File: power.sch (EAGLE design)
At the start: 22 parts

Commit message: change all the things
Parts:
- removed TP1, TP2, TP3, TP4: TPPAD1-13Y, testpad:TPPAD1-13Y
- added BAT+, BAT-, H1, H2, PV+, PV-: MOUNT-PAD-ROUND2.8, holes:MOUNT-PAD-ROUND2.8
- added R10: 1k, rcl:R-US_R0603
- added R9: 47k, rcl:R-US_R0603
- R1, R2: value (none) -> 0R1
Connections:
- new net N$18: R10.2, R9.2, U$6.AIN4
- new net N$8: R9.1
- net GND: now also H1.MOUNT, H2.MOUNT, R10.1
- net N$14: now also BAT-.MOUNT; no longer TP4.TP
- net N$16: now also PV-.MOUNT; no longer TP2.TP
- net N$3: now also PV+.MOUNT, U$3.P$2; no longer TP1.TP, U$3.P$1
- net N$6: now also U$3.P$1; no longer U$3.P$2
- net N$7: now also BAT+.MOUNT; no longer TP3.TP
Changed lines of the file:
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@@
 </classes>
 <parts>
-<part name="TP1" library="testpad" deviceset="TP" device="PAD1-13Y"/>
-<part name="TP2" library="testpad" deviceset="TP" device="PAD1-13Y"/>
-<part name="TP3" library="testpad" deviceset="TP" device="PAD1-13Y"/>
-<part name="TP4" library="testpad" deviceset="TP" device="PAD1-13Y"/>
 <part name="D1" library="diode" deviceset="BY500" device=""/>
 <part name="D2" library="diode" deviceset="BY500" device=""/>
@@
 <part name="U$1" library="mjg" deviceset="FDB6670AL" device=""/>
 <part name="U$2" library="mjg" deviceset="FDB6670AL" device=""/>
-<part name="R1" library="rcl" deviceset="R-US_" device="R0603"/>
-<part name="R2" library="rcl" deviceset="R-US_" device="R0603"/>
+<part name="R1" library="rcl" deviceset="R-US_" device="R0603" value="0R1"/>
+<part name="R2" library="rcl" deviceset="R-US_" device="R0603" value="0R1"/>
 <part name="U$3" library="chokes" deviceset="PLH10AN2211R5P2B" device=""/>
 <part name="U$4" library="chokes" deviceset="TLF14CBH3321R0K1" device=""/>
@@
 <part name="R8" library="rcl" deviceset="R-US_" device="R0603" value="1k"/>
 <part name="GND4" library="supply1" deviceset="GND" device=""/>
+<part name="R9" library="rcl" deviceset="R-US_" device="R0603" value="47k"/>
+<part name="R10" library="rcl" deviceset="R-US_" device="R0603" value="1k"/>
+<part name="GND5" library="supply1" deviceset="GND" device=""/>
+<part name="PV+" library="holes" deviceset="MOUNT-PAD-ROUND" device="2.8"/>
+<part name="PV-" library="holes" deviceset="MOUNT-PAD-ROUND" device="2.8"/>
+<part name="BAT+" library="holes" deviceset="MOUNT-PAD-ROUND" device="2.8"/>
+<part name="BAT-" library="holes" deviceset="MOUNT-PAD-ROUND" device="2.8"/>
+<part name="H1" library="holes" deviceset="MOUNT-PAD-ROUND" device="2.8"/>
+<part name="H2" library="holes" deviceset="MOUNT-PAD-ROUND" device="2.8"/>
+<part name="GND6" library="supply1" deviceset="GND" device=""/>
 </parts>
 <sheets>
@@
 </plain>
 <instances>
-<instance part="TP1" gate="G$1" x="2.54" y="43.18" rot="R90"/>
-<instance part="TP2" gate="G$1" x="-12.7" y="5.08" rot="R90"/>
-<instance part="TP3" gate="G$1" x="96.52" y="58.42" rot="R270"/>
-<instance part="TP4" gate="G$1" x="96.52" y="50.8" rot="R270"/>
 <instance part="D1" gate="1" x="58.42" y="76.2"/>
 <instance part="D2" gate="1" x="58.42" y="71.12"/>
@@
 <instance part="R8" gate="G$1" x="66.04" y="17.78" rot="R180"/>
 <instance part="GND4" gate="1" x="76.2" y="15.24"/>
+<instance part="R9" gate="G$1" x="2.54" y="-7.62" rot="R180"/>
+<instance part="R10" gate="G$1" x="2.54" y="-15.24" rot="R180"/>
+<instance part="GND5" gate="1" x="12.7" y="-17.78"/>
+<instance part="PV+" gate="G$1" x="0" y="43.18" rot="R180"/>
+<instance part="PV-" gate="G$1" x="-12.7" y="5.08" rot="R180"/>
+<instance part="BAT+" gate="G$1" x="96.52" y="58.42"/>
+<instance part="BAT-" gate="G$1" x="96.52" y="50.8"/>
+<instance part="H1" gate="G$1" x="83.82" y="76.2"/>
+<instance part="H2" gate="G$1" x="83.82" y="71.12"/>
+<instance part="GND6" gate="1" x="78.74" y="66.04"/>
 </instances>
 <busses>
@@
 <net name="N$3" class="0">
 <segment>
-<pinref part="TP1" gate="G$1" pin="TP"/>
-<wire x1="12.7" y1="43.18" x2="7.62" y2="43.18" width="0.1524" layer="91"/>
-<pinref part="U$3" gate="G$1" pin="P$1"/>
 <pinref part="R3" gate="G$1" pin="1"/>
-<wire x1="7.62" y1="43.18" x2="5.08" y2="43.18" width="0.1524" layer="91"/>
-<wire x1="7.62" y1="43.18" x2="7.62" y2="33.02" width="0.1524" layer="91"/>
+<wire x1="7.62" y1="43.18" x2="2.54" y2="43.18" width="0.1524" layer="91"/>
+<wire x1="7.62" y1="43.18" x2="7.62" y2="40.64" width="0.1524" layer="91"/>
+<wire x1="7.62" y1="40.64" x2="7.62" y2="33.02" width="0.1524" layer="91"/>
 <wire x1="7.62" y1="33.02" x2="2.54" y2="33.02" width="0.1524" layer="91"/>
-<junction x="7.62" y="43.18"/>
+<wire x1="7.62" y1="40.64" x2="22.86" y2="40.64" width="0.1524" layer="91"/>
+<junction x="7.62" y="40.64"/>
+<pinref part="U$3" gate="G$1" pin="P$2"/>
+<wire x1="22.86" y1="40.64" x2="22.86" y2="43.18" width="0.1524" layer="91"/>
+<pinref part="PV+" gate="G$1" pin="MOUNT"/>
 </segment>
 </net>
@@
 <net name="N$14" class="0">
 <segment>
-<pinref part="TP4" gate="G$1" pin="TP"/>
 <pinref part="R1" gate="G$1" pin="2"/>
 <wire x1="88.9" y1="50.8" x2="91.44" y2="50.8" width="0.1524" layer="91"/>
@@
 <wire x1="91.44" y1="50.8" x2="91.44" y2="-30.48" width="0.1524" layer="91"/>
 <wire x1="91.44" y1="-30.48" x2="124.46" y2="-30.48" width="0.1524" layer="91"/>
+<pinref part="BAT-" gate="G$1" pin="MOUNT"/>
 </segment>
 </net>
@@
 <net name="N$6" class="0">
 <segment>
-<pinref part="U$3" gate="G$1" pin="P$2"/>
-<wire x1="22.86" y1="43.18" x2="27.94" y2="43.18" width="0.1524" layer="91"/>
 <pinref part="U$5" gate="G$1" pin="P$2"/>
 <wire x1="30.48" y1="55.88" x2="27.94" y2="55.88" width="0.1524" layer="91"/>
 <wire x1="27.94" y1="55.88" x2="27.94" y2="45.72" width="0.1524" layer="91"/>
 <pinref part="U$4" gate="G$1" pin="P$1"/>
-<wire x1="27.94" y1="45.72" x2="27.94" y2="43.18" width="0.1524" layer="91"/>
 <wire x1="27.94" y1="45.72" x2="30.48" y2="45.72" width="0.1524" layer="91"/>
 <junction x="27.94" y="45.72"/>
+<wire x1="27.94" y1="45.72" x2="27.94" y2="38.1" width="0.1524" layer="91"/>
+<wire x1="27.94" y1="38.1" x2="12.7" y2="38.1" width="0.1524" layer="91"/>
+<pinref part="U$3" gate="G$1" pin="P$1"/>
+<wire x1="12.7" y1="38.1" x2="12.7" y2="43.18" width="0.1524" layer="91"/>
 </segment>
 </net>
@@
 <pinref part="GND4" gate="1" pin="GND"/>
 </segment>
+<segment>
+<pinref part="R10" gate="G$1" pin="1"/>
+<wire x1="7.62" y1="-15.24" x2="12.7" y2="-15.24" width="0.1524" layer="91"/>
+<pinref part="GND5" gate="1" pin="GND"/>
+</segment>
+<segment>
+<pinref part="H1" gate="G$1" pin="MOUNT"/>
+<pinref part="GND6" gate="1" pin="GND"/>
+<wire x1="81.28" y1="76.2" x2="78.74" y2="76.2" width="0.1524" layer="91"/>
+<wire x1="78.74" y1="76.2" x2="78.74" y2="71.12" width="0.1524" layer="91"/>
+<pinref part="H2" gate="G$1" pin="MOUNT"/>
+<wire x1="78.74" y1="71.12" x2="78.74" y2="68.58" width="0.1524" layer="91"/>
+<wire x1="81.28" y1="71.12" x2="78.74" y2="71.12" width="0.1524" layer="91"/>
+<junction x="78.74" y="71.12"/>
+</segment>
 </net>
 <net name="N$4" class="0">
@@
 <wire x1="-5.08" y1="5.08" x2="-2.54" y2="5.08" width="0.1524" layer="91"/>
 <wire x1="-5.08" y1="-7.62" x2="-5.08" y2="5.08" width="0.1524" layer="91"/>
-<pinref part="TP2" gate="G$1" pin="TP"/>
 <wire x1="-5.08" y1="5.08" x2="-10.16" y2="5.08" width="0.1524" layer="91"/>
 <junction x="-5.08" y="5.08"/>
+<pinref part="PV-" gate="G$1" pin="MOUNT"/>
 </segment>
 </net>
@@
 <pinref part="D1" gate="1" pin="C"/>
 <wire x1="60.96" y1="76.2" x2="68.58" y2="76.2" width="0.1524" layer="91"/>
-<pinref part="TP3" gate="G$1" pin="TP"/>
 <wire x1="68.58" y1="76.2" x2="68.58" y2="71.12" width="0.1524" layer="91"/>
 <pinref part="D2" gate="1" pin="C"/>
@@
 <wire x1="76.2" y1="25.4" x2="76.2" y2="58.42" width="0.1524" layer="91"/>
 <junction x="76.2" y="58.42"/>
+<pinref part="BAT+" gate="G$1" pin="MOUNT"/>
 </segment>
 </net>
@@
 </segment>
 </net>
+<net name="N$8" class="0">
+<segment>
+<pinref part="R9" gate="G$1" pin="1"/>
+<wire x1="12.7" y1="-7.62" x2="7.62" y2="-7.62" width="0.1524" layer="91"/>
+<wire x1="12.7" y1="-7.62" x2="12.7" y2="5.08" width="0.1524" layer="91"/>
+</segment>
+</net>
+<net name="N$18" class="0">
+<segment>
+<wire x1="-2.54" y1="-10.16" x2="109.22" y2="-10.16" width="0.1524" layer="91"/>
+<pinref part="U$6" gate="G$1" pin="AIN4"/>
+<wire x1="109.22" y1="-10.16" x2="109.22" y2="-25.4" width="0.1524" layer="91"/>
+<wire x1="109.22" y1="-25.4" x2="124.46" y2="-25.4" width="0.1524" layer="91"/>
+<pinref part="R9" gate="G$1" pin="2"/>
+<wire x1="-2.54" y1="-7.62" x2="-2.54" y2="-10.16" width="0.1524" layer="91"/>
+<pinref part="R10" gate="G$1" pin="2"/>
+<wire x1="-2.54" y1="-15.24" x2="-2.54" y2="-10.16" width="0.1524" layer="91"/>
+<junction x="-2.54" y="-10.16"/>
+</segment>
+</net>

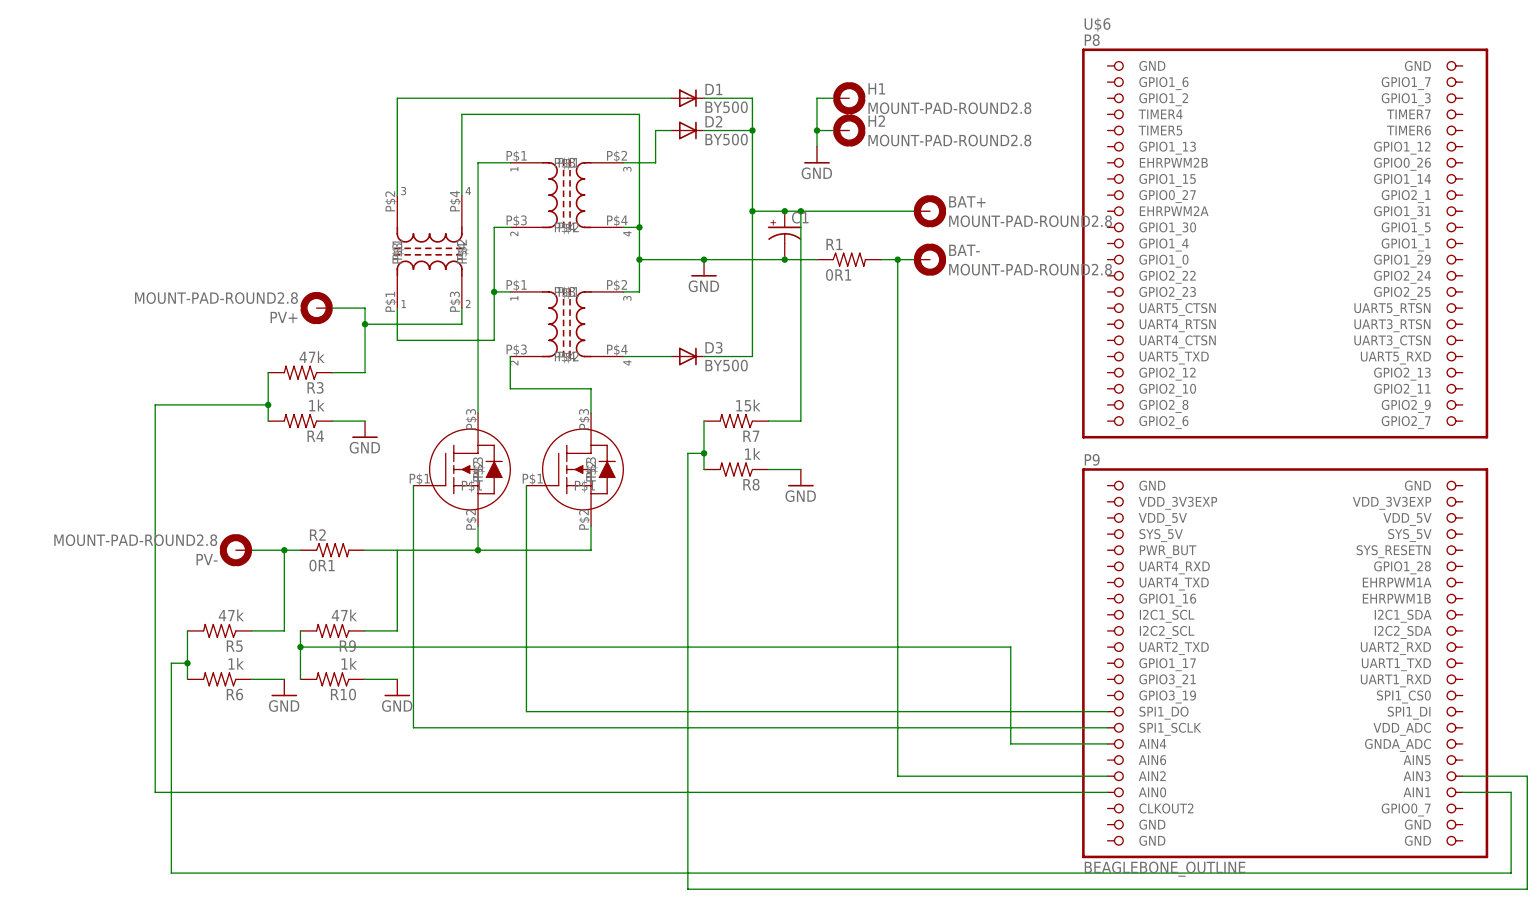
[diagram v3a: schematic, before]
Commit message: schematic might be correct.  board is routed.  no idea if it's routed well.
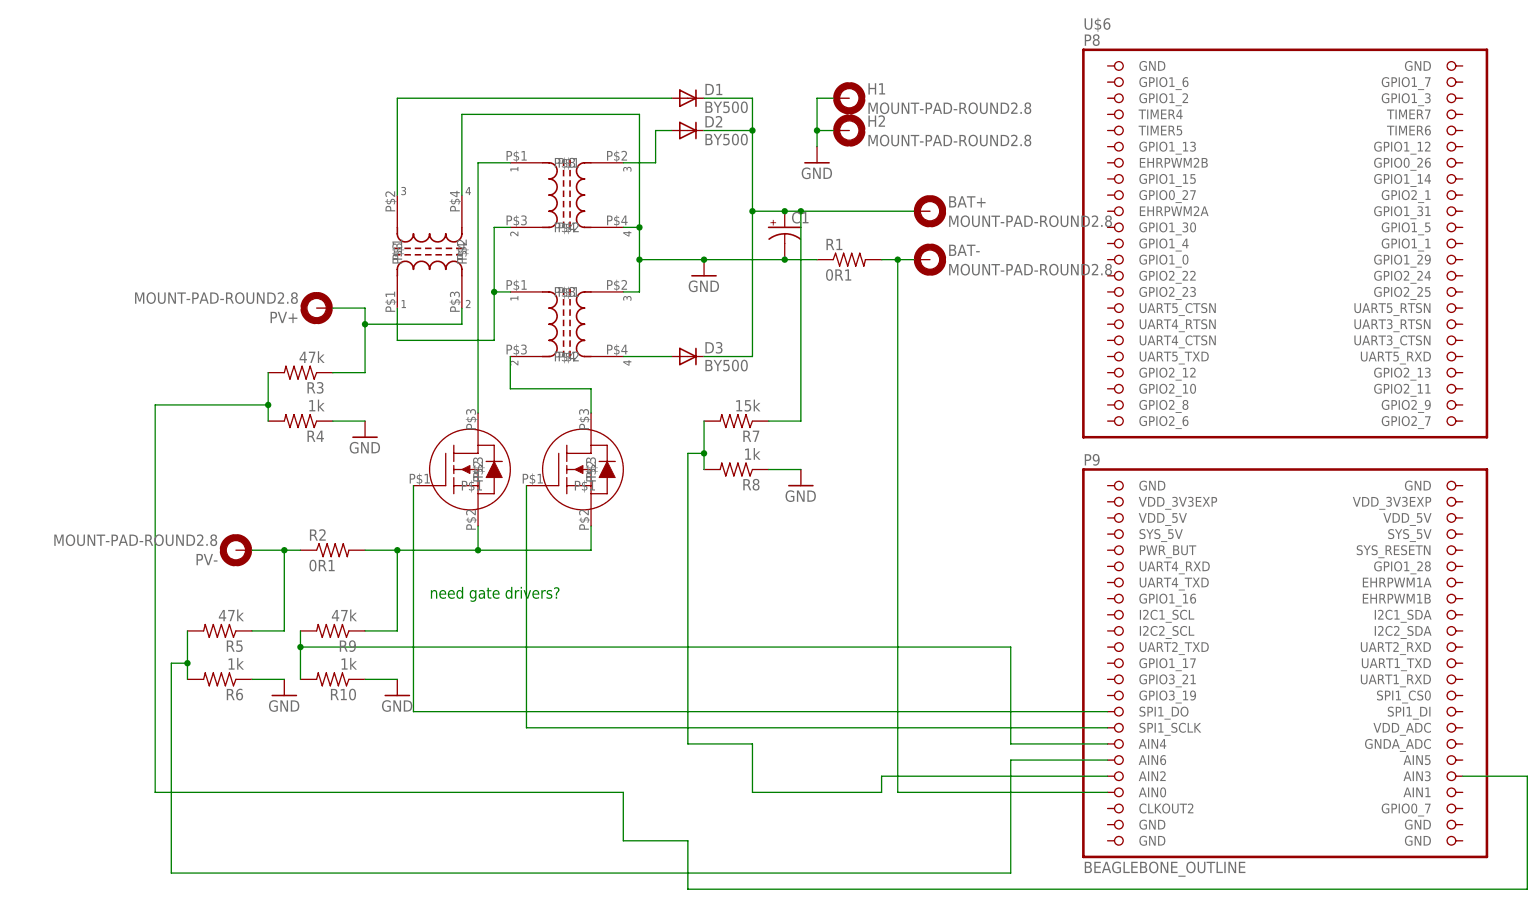
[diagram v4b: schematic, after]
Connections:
- removed net N$14: BAT-.MOUNT, R1.2, U$6.AIN2
- net N$10: now also U$6.AIN2; no longer U$6.AIN3
- net N$11: now also U$2.P$1, U$6.SPI1_SCLK; no longer R2.2, U$1.P$3, U$2.P$3
- net N$12: now also BAT-.MOUNT, R1.2, U$6.AIN0; no longer U$1.P$1, U$6.SPI1_SCLK
- net N$13: now also U$1.P$1; no longer U$2.P$1
- net N$17: now also U$6.AIN6; no longer U$6.AIN1
- net N$4: now also U$6.AIN3; no longer U$6.AIN0
- net N$8: now also R2.2, U$1.P$3, U$2.P$3
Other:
- note added: "need gate drivers?"
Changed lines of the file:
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@@
 <sheet>
 <plain>
+<text x="17.78" y="-2.54" size="1.778" layer="91">need gate drivers?</text>
 </plain>
 <instances>
@@
 </segment>
 </net>
-<net name="N$11" class="0">
-<segment>
-<pinref part="U$1" gate="G$1" pin="P$3"/>
-<wire x1="25.4" y1="8.89" x2="25.4" y2="5.08" width="0.1524" layer="91"/>
-<wire x1="25.4" y1="5.08" x2="43.18" y2="5.08" width="0.1524" layer="91"/>
-<pinref part="U$2" gate="G$1" pin="P$3"/>
-<wire x1="43.18" y1="5.08" x2="43.18" y2="8.89" width="0.1524" layer="91"/>
-<wire x1="25.4" y1="5.08" x2="7.62" y2="5.08" width="0.1524" layer="91"/>
-<junction x="25.4" y="5.08"/>
-<pinref part="R2" gate="G$1" pin="2"/>
-</segment>
-</net>
-<net name="N$12" class="0">
+<net name="N$13" class="0">
 <segment>
 <pinref part="U$1" gate="G$1" pin="P$1"/>
-<pinref part="U$6" gate="G$1" pin="SPI1_SCLK"/>
-<wire x1="124.46" y1="-22.86" x2="15.24" y2="-22.86" width="0.1524" layer="91"/>
-<wire x1="15.24" y1="-22.86" x2="15.24" y2="15.24" width="0.1524" layer="91"/>
-</segment>
-</net>
-<net name="N$13" class="0">
-<segment>
-<pinref part="U$2" gate="G$1" pin="P$1"/>
 <pinref part="U$6" gate="G$1" pin="SPI1_DO"/>
-<wire x1="124.46" y1="-20.32" x2="33.02" y2="-20.32" width="0.1524" layer="91"/>
-<wire x1="33.02" y1="-20.32" x2="33.02" y2="15.24" width="0.1524" layer="91"/>
-</segment>
-</net>
-<net name="N$14" class="0">
-<segment>
-<pinref part="R1" gate="G$1" pin="2"/>
-<wire x1="88.9" y1="50.8" x2="91.44" y2="50.8" width="0.1524" layer="91"/>
-<wire x1="91.44" y1="50.8" x2="93.98" y2="50.8" width="0.1524" layer="91"/>
-<junction x="91.44" y="50.8"/>
-<pinref part="U$6" gate="G$1" pin="AIN2"/>
-<wire x1="91.44" y1="50.8" x2="91.44" y2="-30.48" width="0.1524" layer="91"/>
-<wire x1="91.44" y1="-30.48" x2="124.46" y2="-30.48" width="0.1524" layer="91"/>
-<pinref part="BAT-" gate="G$1" pin="MOUNT"/>
+<wire x1="15.24" y1="-20.32" x2="15.24" y2="15.24" width="0.1524" layer="91"/>
+<wire x1="124.46" y1="-20.32" x2="15.24" y2="-20.32" width="0.1524" layer="91"/>
 </segment>
 </net>
@@
 <wire x1="-25.4" y1="27.94" x2="-25.4" y2="-33.02" width="0.1524" layer="91"/>
 <junction x="-7.62" y="27.94"/>
-<pinref part="U$6" gate="G$1" pin="AIN0"/>
-<wire x1="-25.4" y1="-33.02" x2="124.46" y2="-33.02" width="0.1524" layer="91"/>
+<wire x1="-25.4" y1="-33.02" x2="48.26" y2="-33.02" width="0.1524" layer="91"/>
+<wire x1="58.42" y1="-40.64" x2="58.42" y2="-48.26" width="0.1524" layer="91"/>
+<wire x1="58.42" y1="-48.26" x2="190.5" y2="-48.26" width="0.1524" layer="91"/>
+<pinref part="U$6" gate="G$1" pin="AIN3"/>
+<wire x1="190.5" y1="-48.26" x2="190.5" y2="-30.48" width="0.1524" layer="91"/>
+<wire x1="190.5" y1="-30.48" x2="180.34" y2="-30.48" width="0.1524" layer="91"/>
+<wire x1="48.26" y1="-33.02" x2="48.26" y2="-40.64" width="0.1524" layer="91"/>
+<wire x1="48.26" y1="-40.64" x2="58.42" y2="-40.64" width="0.1524" layer="91"/>
 </segment>
 </net>
@@
 <wire x1="-22.86" y1="-12.7" x2="-22.86" y2="-45.72" width="0.1524" layer="91"/>
 <junction x="-20.32" y="-12.7"/>
-<wire x1="-22.86" y1="-45.72" x2="187.96" y2="-45.72" width="0.1524" layer="91"/>
-<wire x1="187.96" y1="-45.72" x2="187.96" y2="-33.02" width="0.1524" layer="91"/>
-<pinref part="U$6" gate="G$1" pin="AIN1"/>
-<wire x1="187.96" y1="-33.02" x2="180.34" y2="-33.02" width="0.1524" layer="91"/>
+<wire x1="-22.86" y1="-45.72" x2="109.22" y2="-45.72" width="0.1524" layer="91"/>
+<wire x1="109.22" y1="-45.72" x2="109.22" y2="-27.94" width="0.1524" layer="91"/>
+<pinref part="U$6" gate="G$1" pin="AIN6"/>
+<wire x1="109.22" y1="-27.94" x2="124.46" y2="-27.94" width="0.1524" layer="91"/>
 </segment>
 </net>
@@
 </segment>
 </net>
-<net name="N$10" class="0">
-<segment>
-<pinref part="R7" gate="G$1" pin="2"/>
-<pinref part="R8" gate="G$1" pin="2"/>
-<wire x1="60.96" y1="25.4" x2="60.96" y2="20.32" width="0.1524" layer="91"/>
-<wire x1="60.96" y1="20.32" x2="60.96" y2="17.78" width="0.1524" layer="91"/>
-<wire x1="60.96" y1="20.32" x2="58.42" y2="20.32" width="0.1524" layer="91"/>
-<junction x="60.96" y="20.32"/>
-<wire x1="58.42" y1="20.32" x2="58.42" y2="-48.26" width="0.1524" layer="91"/>
-<wire x1="58.42" y1="-48.26" x2="190.5" y2="-48.26" width="0.1524" layer="91"/>
-<pinref part="U$6" gate="G$1" pin="AIN3"/>
-<wire x1="190.5" y1="-48.26" x2="190.5" y2="-30.48" width="0.1524" layer="91"/>
-<wire x1="190.5" y1="-30.48" x2="180.34" y2="-30.48" width="0.1524" layer="91"/>
-</segment>
-</net>
 <net name="N$8" class="0">
 <segment>
 <pinref part="R9" gate="G$1" pin="1"/>
 <wire x1="12.7" y1="-7.62" x2="7.62" y2="-7.62" width="0.1524" layer="91"/>
+<pinref part="U$1" gate="G$1" pin="P$3"/>
+<wire x1="25.4" y1="8.89" x2="25.4" y2="5.08" width="0.1524" layer="91"/>
+<wire x1="25.4" y1="5.08" x2="43.18" y2="5.08" width="0.1524" layer="91"/>
+<pinref part="U$2" gate="G$1" pin="P$3"/>
+<wire x1="43.18" y1="5.08" x2="43.18" y2="8.89" width="0.1524" layer="91"/>
+<wire x1="25.4" y1="5.08" x2="12.7" y2="5.08" width="0.1524" layer="91"/>
+<junction x="25.4" y="5.08"/>
+<pinref part="R2" gate="G$1" pin="2"/>
+<wire x1="12.7" y1="5.08" x2="7.62" y2="5.08" width="0.1524" layer="91"/>
 <wire x1="12.7" y1="-7.62" x2="12.7" y2="5.08" width="0.1524" layer="91"/>
+<junction x="12.7" y="5.08"/>
 </segment>
 </net>
@@
 </segment>
 </net>
+<net name="N$11" class="0">
+<segment>
+<pinref part="U$2" gate="G$1" pin="P$1"/>
+<wire x1="33.02" y1="-22.86" x2="33.02" y2="15.24" width="0.1524" layer="91"/>
+<pinref part="U$6" gate="G$1" pin="SPI1_SCLK"/>
+<wire x1="33.02" y1="-22.86" x2="124.46" y2="-22.86" width="0.1524" layer="91"/>
+</segment>
+</net>
+<net name="N$12" class="0">
+<segment>
+<pinref part="U$6" gate="G$1" pin="AIN0"/>
+<wire x1="91.44" y1="-33.02" x2="124.46" y2="-33.02" width="0.1524" layer="91"/>
+<pinref part="BAT-" gate="G$1" pin="MOUNT"/>
+<pinref part="R1" gate="G$1" pin="2"/>
+<wire x1="88.9" y1="50.8" x2="91.44" y2="50.8" width="0.1524" layer="91"/>
+<wire x1="91.44" y1="50.8" x2="93.98" y2="50.8" width="0.1524" layer="91"/>
+<junction x="91.44" y="50.8"/>
+<wire x1="91.44" y1="50.8" x2="91.44" y2="-33.02" width="0.1524" layer="91"/>
+</segment>
+</net>
+<net name="N$10" class="0">
+<segment>
+<pinref part="U$6" gate="G$1" pin="AIN2"/>
+<wire x1="88.9" y1="-30.48" x2="124.46" y2="-30.48" width="0.1524" layer="91"/>
+<wire x1="88.9" y1="-33.02" x2="88.9" y2="-30.48" width="0.1524" layer="91"/>
+<wire x1="68.58" y1="-33.02" x2="88.9" y2="-33.02" width="0.1524" layer="91"/>
+<wire x1="68.58" y1="-25.4" x2="68.58" y2="-33.02" width="0.1524" layer="91"/>
+<pinref part="R8" gate="G$1" pin="2"/>
+<pinref part="R7" gate="G$1" pin="2"/>
+<wire x1="60.96" y1="25.4" x2="60.96" y2="20.32" width="0.1524" layer="91"/>
+<wire x1="60.96" y1="20.32" x2="60.96" y2="17.78" width="0.1524" layer="91"/>
+<junction x="60.96" y="20.32"/>
+<wire x1="60.96" y1="20.32" x2="58.42" y2="20.32" width="0.1524" layer="91"/>
+<wire x1="58.42" y1="20.32" x2="58.42" y2="-25.4" width="0.1524" layer="91"/>
+<wire x1="58.42" y1="-25.4" x2="68.58" y2="-25.4" width="0.1524" layer="91"/>
+</segment>
+</net>
